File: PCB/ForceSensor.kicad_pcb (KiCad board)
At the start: 2 copper layers, 53.3 x 67.3 mm, 21 parts, among them J2 Conn_01x08, J3 Conn_01x06, J4 Conn_01x10, J5 Conn_01x08, J7 Conn_02x03_Counter_Clockwise, J8 Conn_02x03_Counter_Clockwise

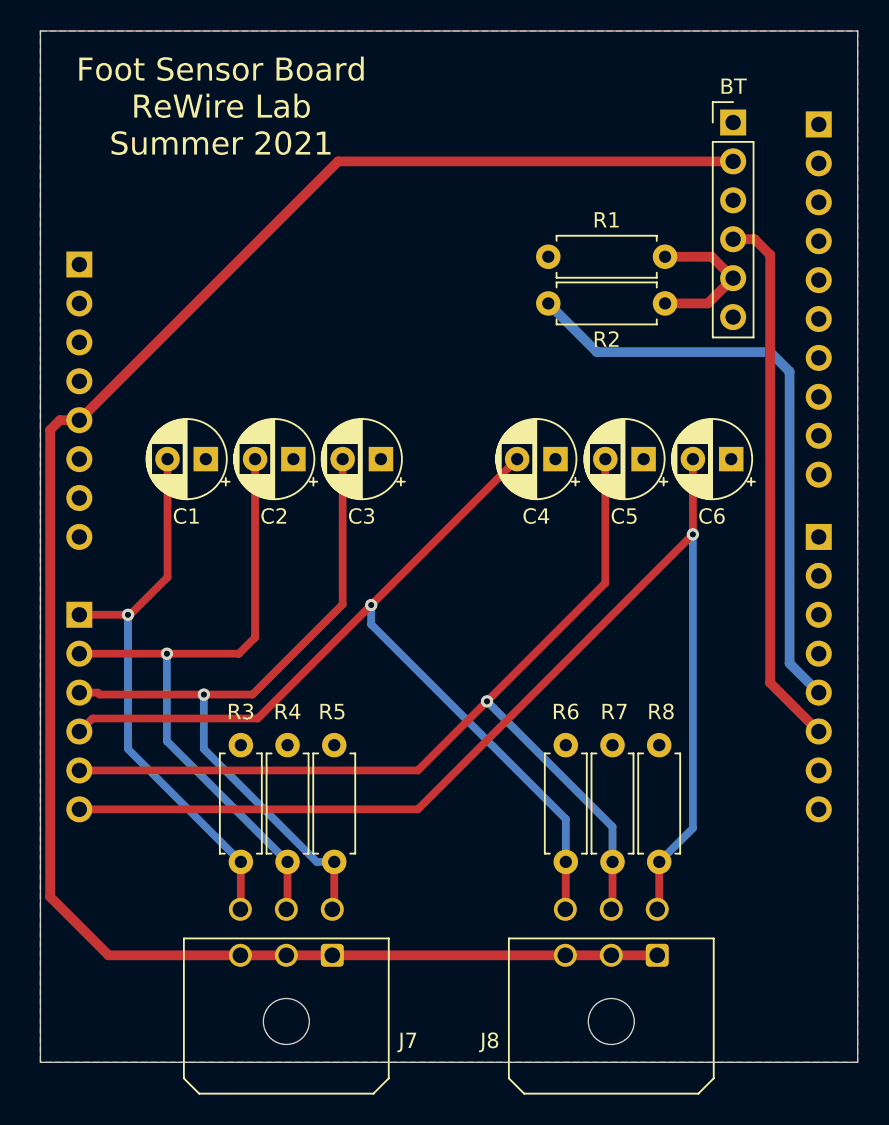
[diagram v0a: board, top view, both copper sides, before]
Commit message: Edits for tolerances
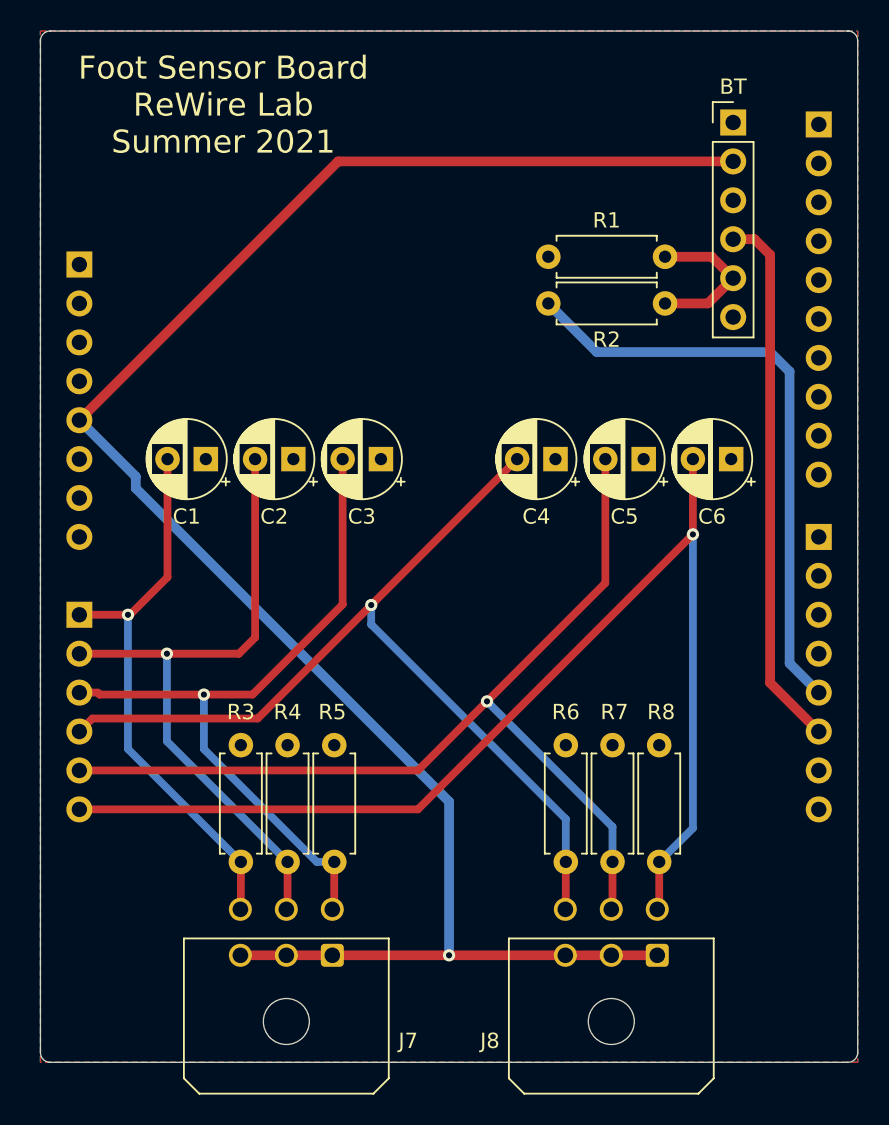
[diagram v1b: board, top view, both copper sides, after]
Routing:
- net +5V: track 123.5 -> 121.9 mm, vias 0 -> 1
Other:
- outline, holes or cut-outs redrawn

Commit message: Added power LED
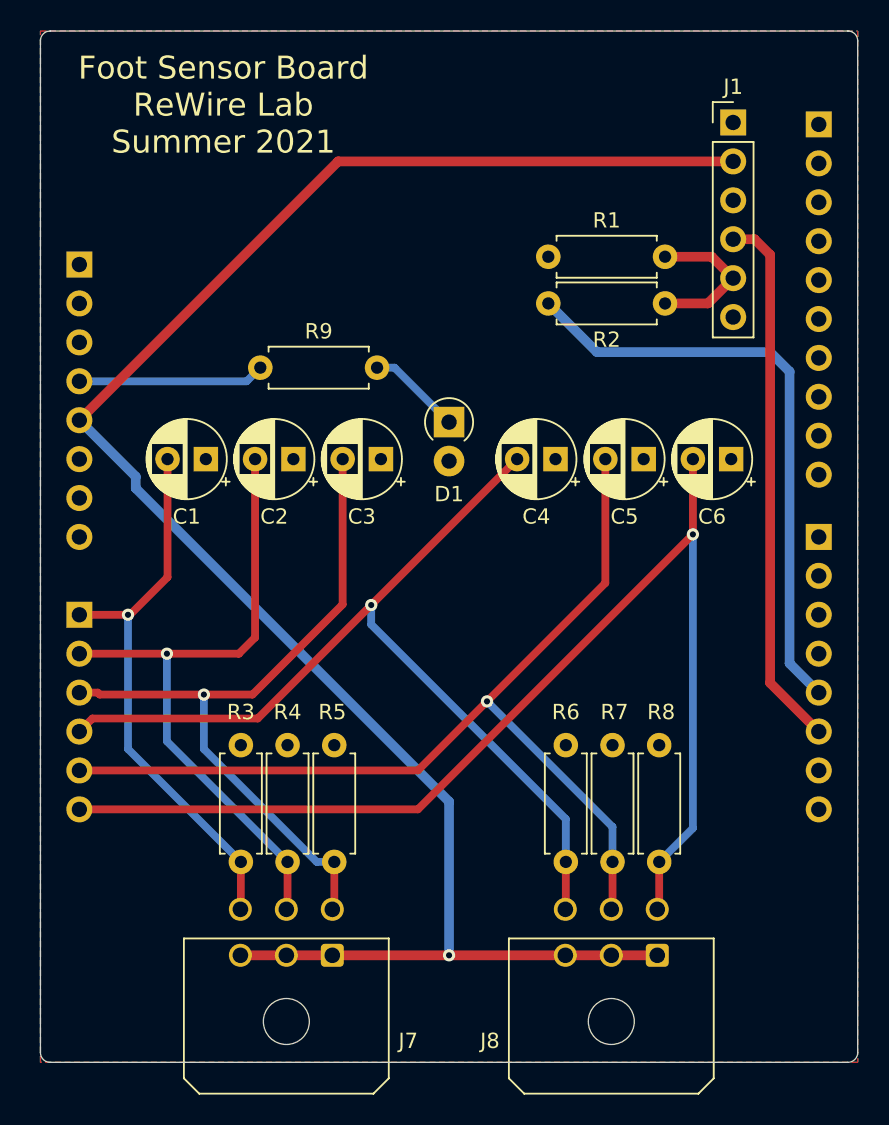
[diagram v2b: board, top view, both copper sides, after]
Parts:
- added D1: LED, Diode_THT:D_T-1_P2.54mm_Vertical_AnodeUp, F.Cu at (236.9, 68.1)
- added R9: 5K Ohm, Resistor_THT:R_Axial_DIN0207_L6.3mm_D2.5mm_P7.62mm_Horizontal, F.Cu at (224.5, 64.5)
- renumbered BT to J1
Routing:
- net +3V3: track 0.00 -> 12.2 mm
- net Net-(D1-Pad1): track 0.00 -> 6.17 mm
